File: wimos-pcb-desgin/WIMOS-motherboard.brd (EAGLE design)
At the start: 130.6 x 117.3 mm, 32 parts

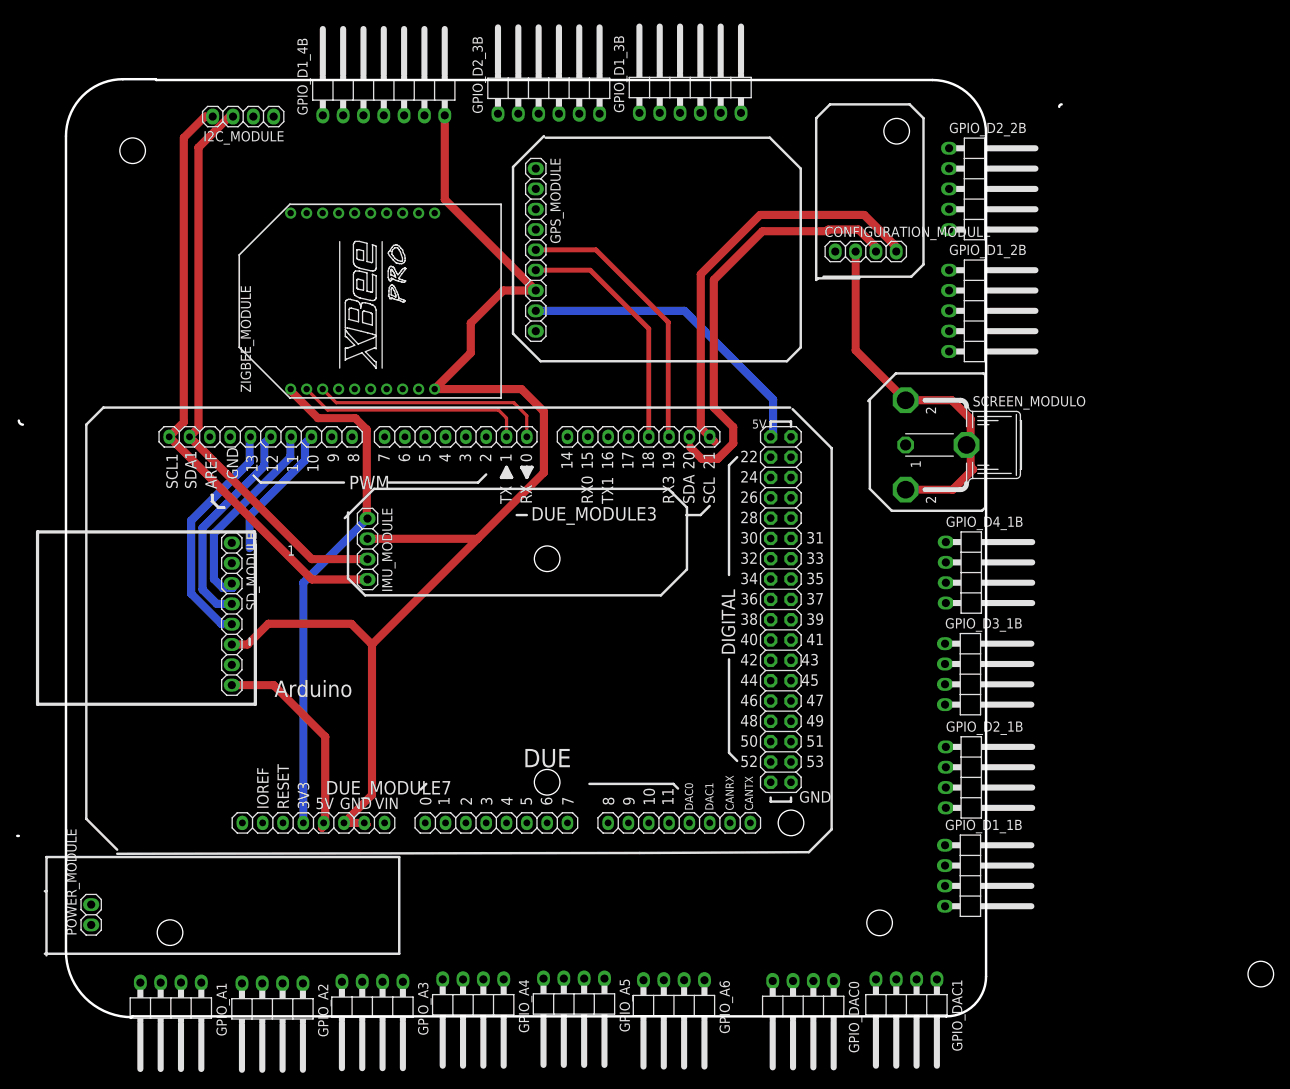
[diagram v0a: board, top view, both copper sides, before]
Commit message: Diseño de la placa pcb del sistema
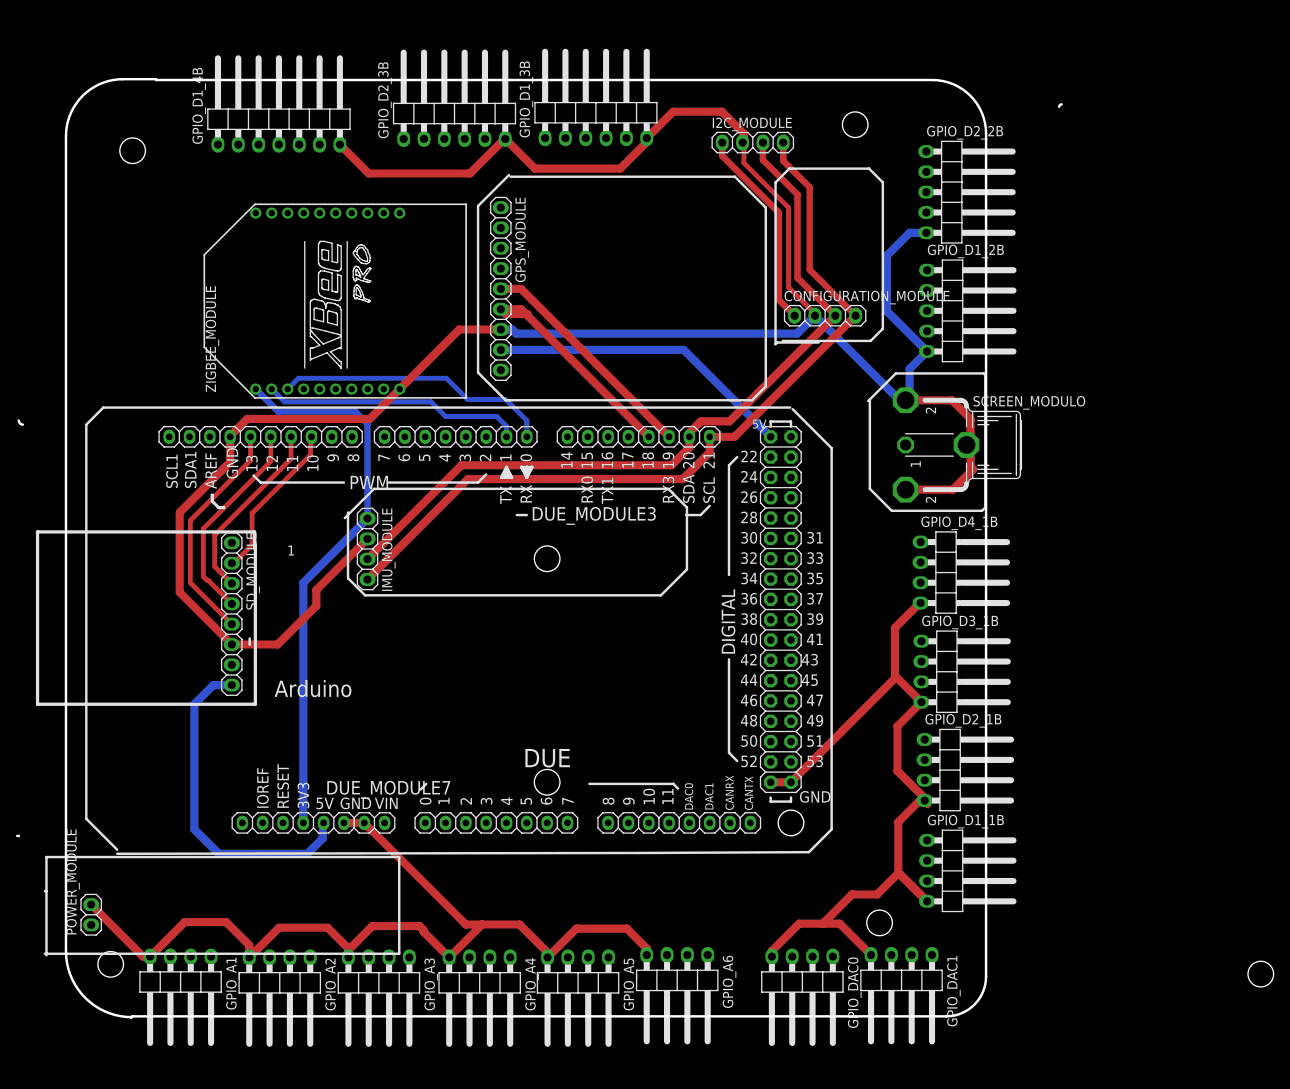
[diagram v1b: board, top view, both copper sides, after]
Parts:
- moved I2C_MODULE 63.8 mm to (91.7, 87.6), turned to 0 degrees
- moved GPIO_D1_4B 13.6 mm to (32.5, 91.1)
- moved GPIO_D1_3B 12.2 mm to (72.1, 91.9)
- moved GPIO_D2_3B 12.2 mm to (54.5, 91.8)
- moved CONFIGURATION_MODULE 9.50 mm to (100.8, 65.9)
- moved GPS_MODULE 6.55 mm to (60.2, 69.3)
- moved ZIGBEE_MODULE 4.37 mm to (38.6, 67.8)
- moved GPIO_A1 3.47 mm to (20.2, -18.0)
- moved GPIO_A2 3.38 mm to (32.6, -18.1)
- moved GPIO_A6 3.18 mm to (82.3, -17.8)
- moved GPIO_A3 3.15 mm to (45.0, -18.1)
- moved GPIO_D4_1B 3.15 mm to (116.5, 33.8)
- moved GPIO_DAC1 3.11 mm to (110.3, -17.8)
- moved GPIO_DAC0 3.05 mm to (97.9, -18.0)
- moved GPIO_D3_1B 2.96 mm to (116.6, 21.4)
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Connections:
- removed net <NONE>: DUE_MODULE1.7
- net DUE_SCL: now also I2C_MODULE.4, IMU_MODULE.4
- net DUE_SCL1: no longer I2C_MODULE.4, IMU_MODULE.4
- net DUE_SDA: now also I2C_MODULE.3, IMU_MODULE.3
- net DUE_SDA1: no longer I2C_MODULE.3, IMU_MODULE.3
- net GND: now also DUE_MODULE1.7
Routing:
- net GND: track 207.5 -> 505.1 mm
- net DUE_SCL1: track 75.0 -> 0.00 mm
- net DUE_SDA1: track 71.1 -> 0.00 mm
- net DUE_SCL: track 51.4 -> 101.2 mm
- net DUE_SDA: track 53.9 -> 97.5 mm
- net I2C_VCC: track 0.00 -> 25.4 mm
- net DUE_5V: track 26.6 -> 41.4 mm
- net DUE_RX1: track 34.7 -> 28.7 mm
- net DUE_RX0: track 29.5 -> 34.7 mm
- net DUE_3.3V: track 64.3 -> 69.0 mm
- net DUE_TX0: track 28.8 -> 32.6 mm
- net DUE_PIN10: track 17.1 -> 20.6 mm
- net DUE_PIN11: track 25.2 -> 23.2 mm
- net DUE_TX1: track 30.7 -> 28.7 mm
- net DUE_PIN12: track 27.0 -> 25.9 mm
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
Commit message: Placa de circuito impreso
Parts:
- removed GPIO_A1, GPIO_A2, GPIO_A3, GPIO_A4, GPIO_A5, GPIO_A6: (no value), pinhead:1X04/90
- added GPIO_A1_1B, GPIO_A2_1B, GPIO_A3_1B, GPIO_A4_1B: (no value), pinhead:1X03/90
- added GPIO_A1_3B: (no value), pinhead:1X05/90
- added IC1: 7805T, linear:TO220H
- added SERIE_MODULE: (no value), pinhead:1X04/90
- GPIO_D1_1B, GPIO_D2_1B, GPIO_D3_1B, GPIO_D4_1B, GPIO_DAC0, GPIO_DAC1: device pinhead:1X04/90 -> pinhead:1X03/90
- GPIO_D1_2B, GPIO_D2_2B: device pinhead:1X05/90 -> pinhead:1X04/90
- GPIO_D1_3B, GPIO_D2_3B: device pinhead:1X06/90 -> pinhead:1X05/90
- GPIO_D1_4B: device pinhead:1X07/90 -> pinhead:1X06/90
- I2C_MODULE: device pinhead:1X04 -> pinhead:1X04/90
- POWER_MODULE: device pinhead:1X02 -> con-jack:DCJ0303
- moved GPIO_D1_4B 116.6 mm to (107.5, 1.83), turned to 270 degrees
- moved GPIO_D1_1B 113.4 mm to (32.4, 71.6), turned to 0 degrees
- moved SCREEN_MODULO 100.1 mm to (14.0, 61.6), flipped to the bottom
- moved GPIO_D2_1B 97.4 mm to (42.5, 71.7), turned to 0 degrees
- moved GPIO_D2_3B 88.9 mm to (107.8, 20.7), turned to 270 degrees
- moved CONFIGURATION_MODULE 86.4 mm to (23.6, 27.2), flipped to the bottom, turned to 270 degrees
- moved GPIO_D3_1B 81.4 mm to (52.8, 71.9), turned to 0 degrees
- moved GPIO_D1_3B 66.3 mm to (107.5, 35.9), turned to 270 degrees
- moved GPIO_D4_1B 65.7 mm to (63.2, 72.2), turned to 0 degrees
- moved GPS_MODULE 48.2 mm to (78.0, 24.5), flipped to the bottom, turned to 180 degrees
- moved ZIGBEE_MODULE 41.0 mm to (73.6, 46.3), flipped to the bottom, turned to 270 degrees
- moved GPIO_D1_2B 40.6 mm to (77.1, 71.9), turned to 0 degrees
- moved I2C_MODULE 40.2 mm to (107.2, 50.5), turned to 270 degrees
- moved SD_MODULE 29.3 mm to (30.1, 57.7), flipped to the bottom, turned to 0 degrees
- moved GPIO_D2_2B 28.2 mm to (90.8, 71.6), turned to 0 degrees
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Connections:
- removed net DUE_PIN26: DUE_MODULE4.8
- removed net GPIO_3.3V: GPIO_A1.1, GPIO_A2.1, GPIO_A3.1, GPIO_A4.1, GPIO_A5.1, GPIO_A6.1, GPIO_D1_1B.1, GPIO_D1_2B.1, GPIO_D1_3B.1, GPIO_D1_4B.1, GPIO_D2_1B.1, GPIO_D2_2B.1, GPIO_D2_3B.1, GPIO_D3_1B.1, GPIO_D4_1B.1, GPIO_DAC0.1, GPIO_DAC1.1
- removed net GPIO_5V: GPIO_A1.2, GPIO_A2.2, GPIO_A3.2, GPIO_A4.2, GPIO_A5.2, GPIO_A6.2, GPIO_D1_1B.2, GPIO_D1_2B.2, GPIO_D1_3B.2, GPIO_D1_4B.2, GPIO_D2_1B.2, GPIO_D2_2B.2, GPIO_D2_3B.2, GPIO_D3_1B.2, GPIO_D4_1B.2, GPIO_DAC0.2, GPIO_DAC1.2
- removed net GPIO_A1: GPIO_A1.3
- removed net GPIO_A2: GPIO_A2.3
- removed net GPIO_A3: GPIO_A3.3
- removed net GPIO_A4: GPIO_A4.3
- removed net GPIO_A5: GPIO_A5.3
- removed net GPIO_A6: GPIO_A6.3
- removed net GPIO_D1_1B: GPIO_D1_1B.3
- removed net GPIO_D1_2.1B: GPIO_D1_2B.3
- removed net GPIO_D1_2.2B: GPIO_D1_2B.4
- removed net GPIO_D1_3.1B: GPIO_D1_3B.3
- removed net GPIO_D1_3.2B: GPIO_D1_3B.4
- removed net GPIO_D1_3.3B: GPIO_D1_3B.5
- removed net GPIO_D1_4.1B: GPIO_D1_4B.3
- removed net GPIO_D1_4.2B: GPIO_D1_4B.4
- removed net GPIO_D1_4.3B: GPIO_D1_4B.5
- removed net GPIO_D1_4.4B: GPIO_D1_4B.6
- removed net GPIO_D2_1B: GPIO_D2_1B.3
- removed net GPIO_D2_2.1B: GPIO_D2_2B.3
- removed net GPIO_D2_2.2B: GPIO_D2_2B.4
- removed net GPIO_D2_3.1B: GPIO_D2_3B.3
- removed net GPIO_D2_3.2B: GPIO_D2_3B.4
- removed net GPIO_D2_3.3B: GPIO_D2_3B.5
- removed net GPIO_D3_1B: GPIO_D3_1B.3
- removed net GPIO_D4_1B: GPIO_D4_1B.3
- removed net GPIO_DAC0: GPIO_DAC0.3
- removed net GPIO_DAC1: GPIO_DAC1.3
- removed net I2C_VCC: CONFIGURATION_MODULE.1, I2C_MODULE.1
- removed net POWER_VCC: POWER_MODULE.1
- new net 5V: CONFIGURATION_MODULE.1, GPIO_A1_1B.2, GPIO_A1_3B.2, GPIO_A2_1B.2, GPIO_A3_1B.2, GPIO_A4_1B.2, GPIO_D1_1B.2, GPIO_D1_2B.2, GPIO_D1_3B.2, GPIO_D1_4B.2, GPIO_D2_1B.2, GPIO_D2_2B.2, GPIO_D2_3B.2, GPIO_D3_1B.2, GPIO_D4_1B.2, GPIO_DAC0.2, GPIO_DAC1.2, I2C_MODULE.1, IC1.3, SD_MODULE.8
- new net <NONE>: DUE_MODULE1.7
- new net DUE_PIN21: DUE_MODULE4.4
- new net SERIE_RX: SERIE_MODULE.4
- new net SERIE_TX: SERIE_MODULE.3
- new net SERIE_VCC: SERIE_MODULE.1
- new net VCC: IC1.1, POWER_MODULE.1
- net DUE_5V: no longer SD_MODULE.8
- net DUE_A_PIN_1: now also GPIO_A1_1B.3
- net DUE_A_PIN_10: now also GPIO_A1_3B.3
- net DUE_A_PIN_2: now also GPIO_A2_1B.3
- net DUE_A_PIN_3: now also GPIO_A3_1B.3
- net DUE_A_PIN_4: now also GPIO_A4_1B.3
- net DUE_A_PIN_8: now also GPIO_A1_3B.5
- net DUE_A_PIN_9: now also GPIO_A1_3B.4
- net DUE_DAC0: now also GPIO_DAC0.3
- net DUE_DAC1: now also GPIO_DAC1.3
- net DUE_PIN2: now also GPIO_D2_2B.4
- net DUE_PIN22: now also DUE_MODULE4.3; no longer DUE_MODULE4.4
- net DUE_PIN23: now also DUE_MODULE4.6; no longer DUE_MODULE4.3
- net DUE_PIN24: now also DUE_MODULE4.5; no longer DUE_MODULE4.6
- net DUE_PIN25: now also DUE_MODULE4.7; no longer DUE_MODULE4.5
- net DUE_PIN27: now also DUE_MODULE4.8; no longer DUE_MODULE4.7
- net DUE_PIN28: now also DUE_MODULE4.9; no longer DUE_MODULE4.10
- net DUE_PIN29: now also DUE_MODULE4.10; no longer DUE_MODULE4.9
- net DUE_PIN3: now also GPIO_D2_2B.3
- net DUE_PIN30: now also DUE_MODULE4.11; no longer DUE_MODULE4.12
- net DUE_PIN31: now also DUE_MODULE4.12; no longer DUE_MODULE4.11
- net DUE_PIN32: now also DUE_MODULE4.13; no longer DUE_MODULE4.14
- net DUE_PIN33: now also DUE_MODULE4.14; no longer DUE_MODULE4.13
- net DUE_PIN34: now also DUE_MODULE4.15; no longer DUE_MODULE4.16
- net DUE_PIN35: now also DUE_MODULE4.16, GPIO_D1_3B.3; no longer DUE_MODULE4.15
- net DUE_PIN36: now also DUE_MODULE4.17; no longer DUE_MODULE4.18
- net DUE_PIN37: now also DUE_MODULE4.18, GPIO_D1_3B.4; no longer DUE_MODULE4.17
- net DUE_PIN38: now also DUE_MODULE4.19; no longer DUE_MODULE4.20
- net DUE_PIN39: now also DUE_MODULE4.20, GPIO_D1_3B.5; no longer DUE_MODULE4.19
- net DUE_PIN4: now also GPIO_D1_2B.4
- net DUE_PIN40: now also DUE_MODULE4.21; no longer DUE_MODULE4.22
- net DUE_PIN41: now also DUE_MODULE4.22, GPIO_D2_3B.3; no longer DUE_MODULE4.21
- net DUE_PIN42: now also DUE_MODULE4.23; no longer DUE_MODULE4.24
- net DUE_PIN43: now also DUE_MODULE4.24, GPIO_D2_3B.4; no longer DUE_MODULE4.23
- net DUE_PIN44: now also DUE_MODULE4.25; no longer DUE_MODULE4.26
- net DUE_PIN45: now also DUE_MODULE4.26, GPIO_D2_3B.5; no longer DUE_MODULE4.25
- net DUE_PIN46: now also DUE_MODULE4.27; no longer DUE_MODULE4.28
- net DUE_PIN47: now also DUE_MODULE4.28, GPIO_D1_4B.3; no longer DUE_MODULE4.27
- net DUE_PIN48: now also DUE_MODULE4.29; no longer DUE_MODULE4.30
- net DUE_PIN49: now also DUE_MODULE4.30, GPIO_D1_4B.4; no longer DUE_MODULE4.29
- net DUE_PIN5: now also GPIO_D1_2B.3
- net DUE_PIN50: now also DUE_MODULE4.31; no longer DUE_MODULE4.32
- net DUE_PIN51: now also DUE_MODULE4.32, GPIO_D1_4B.5; no longer DUE_MODULE4.31
- net DUE_PIN52: now also DUE_MODULE4.33; no longer DUE_MODULE4.34
- net DUE_PIN53: now also DUE_MODULE4.34, GPIO_D1_4B.6; no longer DUE_MODULE4.33
- net DUE_PIN6: now also GPIO_D4_1B.3
- net DUE_PIN7: now also GPIO_D3_1B.3
- net DUE_PIN8: now also GPIO_D2_1B.3
- net DUE_PIN9: now also GPIO_D1_1B.3
- net GND: now also GPIO_A1_1B.1, GPIO_A1_3B.1, GPIO_A2_1B.1, GPIO_A3_1B.1, GPIO_A4_1B.1, GPIO_D1_1B.1, GPIO_D1_2B.1, GPIO_D1_3B.1, GPIO_D1_4B.1, GPIO_D2_1B.1, GPIO_D2_2B.1, GPIO_D2_3B.1, GPIO_D3_1B.1, GPIO_D4_1B.1, GPIO_DAC0.1, GPIO_DAC1.1, IC1.2, POWER_MODULE.3, SERIE_MODULE.2; no longer DUE_MODULE1.7, GPIO_A1.4, GPIO_A2.4, GPIO_A3.4, GPIO_A4.4, GPIO_A5.4, GPIO_A6.4, GPIO_D1_1B.4, GPIO_D1_2B.5, GPIO_D1_3B.6, GPIO_D1_4B.7, GPIO_D2_1B.4, GPIO_D2_2B.5, GPIO_D2_3B.6, GPIO_D3_1B.4, GPIO_D4_1B.4, GPIO_DAC0.4, GPIO_DAC1.4
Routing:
- net 5V: track 0.00 -> 418.7 mm
- net GND: track 505.1 -> 447.1 mm
- net DUE_PIN3: track 0.00 -> 46.5 mm
- net DUE_PIN2: track 0.00 -> 45.9 mm
- net DUE_A_PIN_1: track 0.00 -> 43.6 mm
- net DUE_5V: track 41.4 -> 0.00 mm
- net DUE_PIN5: track 0.00 -> 39.6 mm
- net DUE_PIN4: track 0.00 -> 38.7 mm
- net DUE_A_PIN_2: track 0.00 -> 34.8 mm
- net DUE_PIN6: track 0.00 -> 29.8 mm
- net DUE_A_PIN_3: track 0.00 -> 26.9 mm
- net DUE_RX0: track 34.7 -> 8.62 mm
- net I2C_VCC: track 25.4 -> 0.00 mm
- net DUE_3.3V: track 69.0 -> 94.1 mm
- net DUE_TX0: track 32.6 -> 8.85 mm
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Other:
- board size 130.6 x 117.3 mm -> 103.3 x 82.9 mm
